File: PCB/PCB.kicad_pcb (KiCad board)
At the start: 2 copper layers, 110 x 80 mm, 109 parts, among them J2 Conn, J3 Screw_Terminal_01x02, J4 Screw_Terminal_01x02, J5 Screw_Terminal_01x02, J6 Screw_Terminal_01x02, Q1 Q_NPN_BCE, Q10 Q_NPN, Q11 Q_PNP_BCE, Q12 Q_NPN, Q13 Q_PNP, Q14 Q_PNP_BCE, Q15 Q_PNP_BCE, Q16 Q-NPN, Q17 Q-NPN, Q18 Q-NPN, Q19 Q-PNP, Q2 Q_PNP_BCE, Q20 Q-NPN, Q21 Q-PNP, Q22 Q-NPN, Q23 Q-PNP, Q24 Q-PNP, Q25 Q-NPN, Q26 Q-NPN, Q27 Q-PNP, Q28 Q-NPN, Q29 Q_PNP, Q3 Q_NPN_BCE, Q4 Q_PNP_BCE, Q5 Q_NPN_BCE, Q6 Q_PNP_BCE, Q7 Q_PNP_BCE, Q8 Q_NPN_BCE, Q9 Q_NPN_BCE

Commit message: update
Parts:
- moved Q2 2.00 mm to (186.0, 93.5), turned to 90 degrees
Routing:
- net Net-(C10-Pad1): track 16.8 -> 24.7 mm
- net Net-(C3-Pad1): track 33.5 -> 31.1 mm
- net Net-(Q2-Pad3): track 3.41 -> 5.24 mm
- net Net-(Q2-Pad1): track 19.2 -> 18.2 mm
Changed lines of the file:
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@@
     (thickness 1.6)
     (drawings 6)
-    (tracks 624)
+    (tracks 630)
     (zones 0)
     (modules 109)
@@
   )
   (setup
-    (last_trace_width 0.8)
+    (last_trace_width 0.4)
     (user_trace_width 0.4)
     (user_trace_width 0.8)
@@
   )
   (module Package_TO_SOT_SMD:SOT-23_Handsoldering (layer F.Cu)
-    (at 186 91.5)
+    (at 186 93.5 90)
     (descr "SOT-23, Handsoldering")
     (tags SOT-23)
     (attr smd)
-    (fp_text reference Q2 (at 0 -2.5) (layer F.SilkS)
+    (fp_text reference Q2 (at 0 -2.5 90) (layer F.SilkS)
       (effects (font (size 1 1) (thickness 0.15)))
     )
-    (fp_text value Q_PNP_BCE (at 0 2.5) (layer F.Fab)
+    (fp_text value Q_PNP_BCE (at 0 2.5 90) (layer F.Fab)
       (effects (font (size 1 1) (thickness 0.15)))
     )
@@
     (fp_line (start 0.76 -1.58) (end 0.76 -0.65) (layer F.SilkS) (width 0.12))
     (fp_line (start 0.76 1.58) (end 0.76 0.65) (layer F.SilkS) (width 0.12))
-    (fp_text user %R (at 0 0 90) (layer F.Fab)
+    (fp_text user %R (at 0 0) (layer F.Fab)
       (effects (font (size 0.5 0.5) (thickness 0.075)))
     )
-    (pad 3 smd rect (at 1.5 0) (size 1.9 0.8) (layers F.Cu F.Paste F.Mask)
+    (pad 3 smd rect (at 1.5 0 90) (size 1.9 0.8) (layers F.Cu F.Paste F.Mask)
       (net 34 "Net-(Q2-Pad3)"))
-    (pad 2 smd rect (at -1.5 0.95) (size 1.9 0.8) (layers F.Cu F.Paste F.Mask)
+    (pad 2 smd rect (at -1.5 0.95 90) (size 1.9 0.8) (layers F.Cu F.Paste F.Mask)
       (net 6 "Net-(C3-Pad1)"))
-    (pad 1 smd rect (at -1.5 -0.95) (size 1.9 0.8) (layers F.Cu F.Paste F.Mask)
+    (pad 1 smd rect (at -1.5 -0.95 90) (size 1.9 0.8) (layers F.Cu F.Paste F.Mask)
       (net 35 "Net-(Q2-Pad1)"))
     (model ${KISYS3DMOD}/Package_TO_SOT_SMD.3dshapes/SOT-23.wrl
@@
   (segment (start 188.8513 97.6013) (end 190.8987 97.6013) (width 0.4) (layer F.Cu) (net 6))
   (segment (start 197.5287 97.6013) (end 190.8987 97.6013) (width 0.8) (layer F.Cu) (net 6))
-  (segment (start 190.8987 97.6013) (end 186.8999 97.6013) (width 0.8) (layer F.Cu) (net 6))
   (segment (start 188.4513 97.6013) (end 188.8513 97.6013) (width 0.8) (layer F.Cu) (net 6))
-  (segment (start 184.5 93.65) (end 188.4513 97.6013) (width 0.8) (layer F.Cu) (net 6))
-  (segment (start 184.5 92.45) (end 184.5 93.65) (width 0.8) (layer F.Cu) (net 6))
+  (segment (start 189.6013 96.4513) (end 189.6013 97.6013) (width 0.8) (layer F.Cu) (net 6))
+  (segment (start 188.15 95) (end 189.6013 96.4513) (width 0.8) (layer F.Cu) (net 6))
+  (segment (start 186.95 95) (end 188.15 95) (width 0.8) (layer F.Cu) (net 6))
+  (segment (start 190.8987 97.6013) (end 189.6013 97.6013) (width 0.8) (layer F.Cu) (net 6))
+  (segment (start 189.6013 97.6013) (end 186.8999 97.6013) (width 0.8) (layer F.Cu) (net 6))
   (segment (start 203.384828 91.991772) (end 204.0082 91.3684) (width 0.8) (layer F.Cu) (net 7))
   (segment (start 203.377428 91.999172) (end 203.384828 91.991772) (width 0.4) (layer F.Cu) (net 7))
@@
   (segment (start 178.4341 104.923) (end 178.405 104.9521) (width 0.4) (layer F.Cu) (net 17))
   (segment (start 178.4341 101.1421) (end 178.4341 104.923) (width 0.8) (layer F.Cu) (net 17))
-  (segment (start 180.5513 99.0249) (end 178.4341 101.1421) (width 0.8) (layer F.Cu) (net 17))
-  (segment (start 180.5513 92.3881) (end 180.5513 99.0249) (width 0.8) (layer F.Cu) (net 17))
   (segment (start 178.4073 101.1153) (end 178.4341 101.1421) (width 0.8) (layer F.Cu) (net 17))
   (segment (start 175.0878 101.1153) (end 178.4073 101.1153) (width 0.8) (layer F.Cu) (net 17))
+  (segment (start 181.5 97.5) (end 178.5 100.5) (width 0.4) (layer F.Cu) (net 17))
+  (segment (start 181.813199 93.649999) (end 185.770001 93.649999) (width 0.4) (layer F.Cu) (net 17))
+  (segment (start 180.5513 92.3881) (end 181.813199 93.649999) (width 0.4) (layer F.Cu) (net 17))
+  (segment (start 185.770001 93.649999) (end 185.850001 93.729999) (width 0.4) (layer F.Cu) (net 17))
+  (segment (start 185.850001 93.729999) (end 185.850001 96.270001) (width 0.4) (layer F.Cu) (net 17))
+  (segment (start 185.850001 96.270001) (end 184.620002 97.5) (width 0.4) (layer F.Cu) (net 17))
+  (segment (start 184.620002 97.5) (end 181.5 97.5) (width 0.4) (layer F.Cu) (net 17))
   (segment (start 257.6872 61.3783) (end 260.5717 61.3783) (width 3) (layer F.Cu) (net 18))
   (segment (start 265.2 56.75) (end 274.7 56.75) (width 3) (layer F.Cu) (net 18))
@@
   (segment (start 184.7423 108.4954) (end 184.7423 104.4441) (width 0.8) (layer F.Cu) (net 33))
   (segment (start 190.7903 91.5) (end 190.8764 91.4139) (width 0.8) (layer F.Cu) (net 34))
-  (segment (start 187.5 91.5) (end 190.7903 91.5) (width 0.8) (layer F.Cu) (net 34))
+  (segment (start 190.2903 92) (end 190.8764 91.4139) (width 0.8) (layer F.Cu) (net 34))
+  (segment (start 186 92) (end 190.2903 92) (width 0.8) (layer F.Cu) (net 34))
   (segment (start 173.1878 95.7675) (end 173.198 95.7573) (width 0.4) (layer F.Cu) (net 35))
   (segment (start 173.1878 101.1153) (end 173.1878 95.7675) (width 0.8) (layer F.Cu) (net 35))
@@
   (segment (start 173.198 95.7573) (end 175.098 95.7573) (width 0.8) (layer F.Cu) (net 35))
   (segment (start 175.098 95.2073) (end 175.098 95.7573) (width 0.4) (layer F.Cu) (net 35))
-  (segment (start 178.89221 91.41309) (end 175.098 95.2073) (width 0.4) (layer F.Cu) (net 35))
-  (segment (start 181.170566 91.41309) (end 178.89221 91.41309) (width 0.4) (layer F.Cu) (net 35))
-  (segment (start 182.033656 90.55) (end 181.170566 91.41309) (width 0.4) (layer F.Cu) (net 35))
-  (segment (start 184.5 90.55) (end 182.033656 90.55) (width 0.4) (layer F.Cu) (net 35))
+  (segment (start 184.2927 95.7573) (end 185.05 95) (width 0.8) (layer F.Cu) (net 35))
+  (segment (start 175.098 95.7573) (end 184.2927 95.7573) (width 0.8) (layer F.Cu) (net 35))
   (segment (start 174.9378 110.3586) (end 174.9669 110.3877) (width 0.4) (layer F.Cu) (net 36))
   (segment (start 174.1378 110.3586) (end 174.9378 110.3586) (width 0.4) (layer F.Cu) (net 36))

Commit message: update pcb
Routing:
- net Net-(Q24-Pad3): track 49.8 -> 36.4 mm
- net Net-(Q19-Pad3): track 31.2 -> 20.7 mm
- net VCC: track 163.6 -> 169.1 mm
- net Net-(Q16-Pad1): track 23.3 -> 28.6 mm
- net Net-(C3-Pad1): track 31.1 -> 27.5 mm
- net GND: vias 1 -> 2

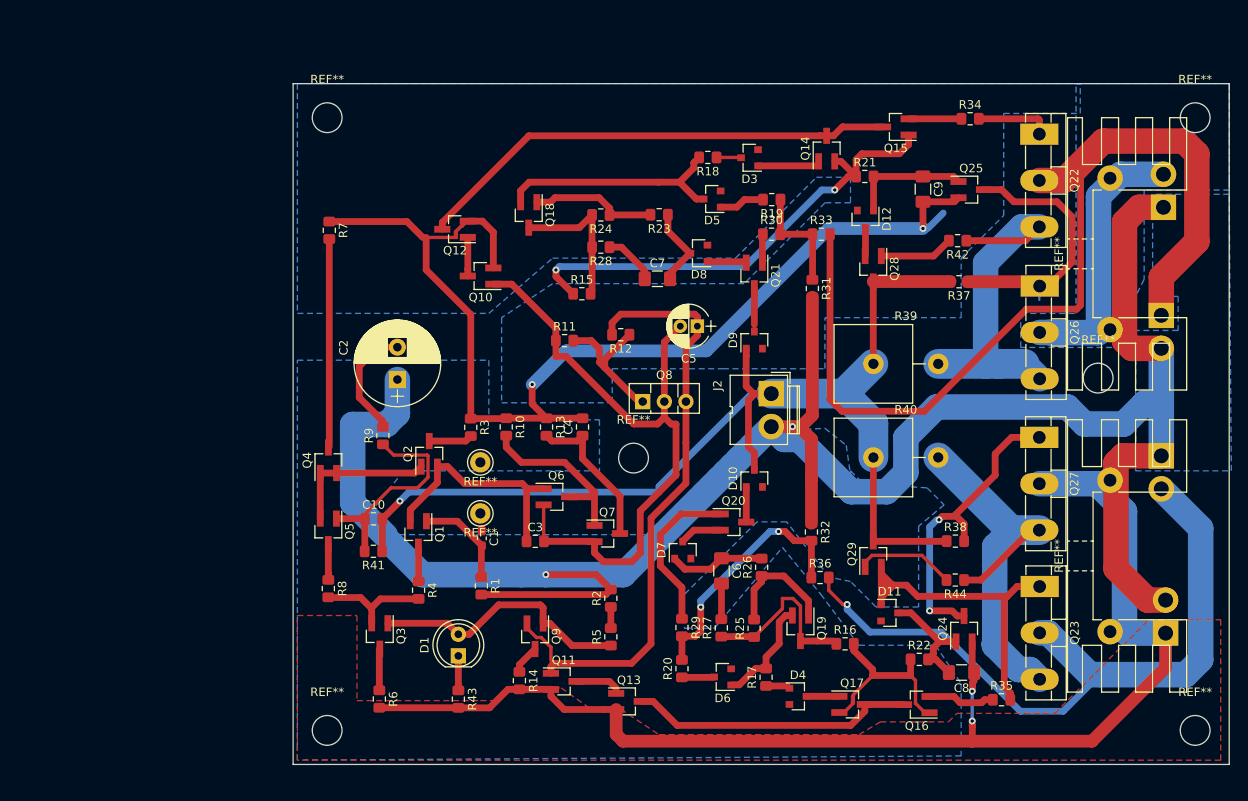
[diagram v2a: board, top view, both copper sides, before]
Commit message: Agregados los capacitores de alimentacion, pistas a las borneras sobre cara superior y a capacitores por cara inferior. Faltaría acomodar los FILL
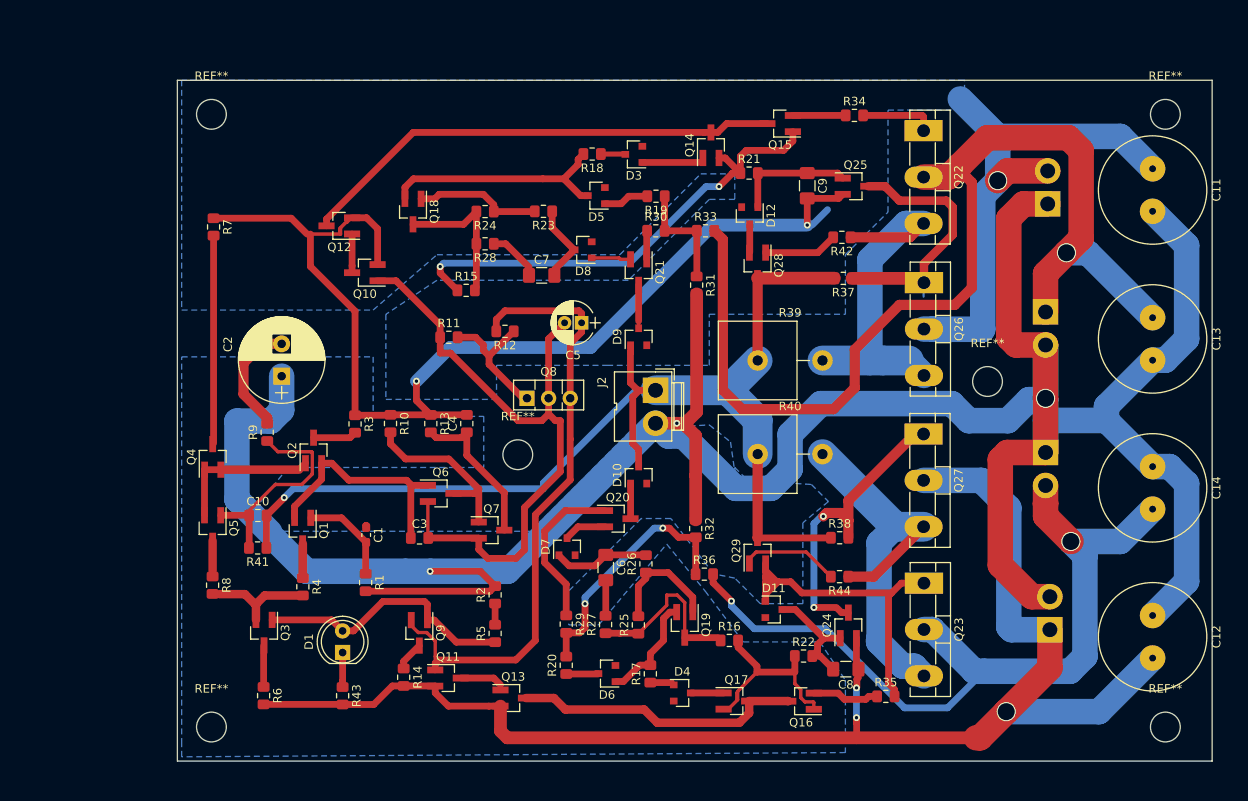
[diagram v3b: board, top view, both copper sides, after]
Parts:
- removed the REF** at (192.0, 94.5)
- removed the REF** at (192.0, 100.5)
- removed the REF** at (266.0, 105.5)
- removed the REF** at (266.0, 70.0)
- added C11: C, Capacitor_THT:C_Radial_D12.5mm_H20.0mm_P5.00mm, F.Cu at (271.0, 60.0)
- added C12: C, Capacitor_THT:C_Radial_D12.5mm_H20.0mm_P5.00mm, F.Cu at (271.0, 112.5)
- added C13: C, Capacitor_THT:C_Radial_D12.5mm_H20.0mm_P5.00mm, F.Cu at (271.0, 77.5)
- added C14: C, Capacitor_THT:C_Radial_D12.5mm_H20.0mm_P5.00mm, F.Cu at (271.0, 95.0)
- moved J4 13.6 mm to (258.9, 114.2)
- moved C1 13.6 mm to (178.6, 103.0)
- moved C10 13.6 mm to (165.9, 100.7)
- moved C3 13.6 mm to (184.9, 103.4)
- moved C5 13.6 mm to (203.9, 78.1)
- moved C7 13.6 mm to (199.2, 72.5)
- moved C8 13.6 mm to (235.0, 118.8)
- moved C9 13.6 mm to (230.4, 62.0)
- moved D10 13.6 mm to (210.6, 96.0)
- moved D12 13.6 mm to (223.7, 65.5)
- moved D3 13.6 mm to (210.0, 58.3)
- moved D4 13.6 mm to (215.7, 121.6)
- moved D5 13.6 mm to (205.6, 63.2)
- moved D6 13.6 mm to (206.9, 119.3)
- moved D7 13.6 mm to (202.2, 104.4)
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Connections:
- J5 pad 1: Net-(J5-Pad1) -> GND
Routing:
- net GND: track 275.0 -> 355.5 mm, vias 2 -> 3
- net VCC: track 169.1 -> 200.1 mm, vias 2 -> 3
- net VEE: track 147.9 -> 167.9 mm, vias 2 -> 3
- net +15V: track 112.7 -> 129.1 mm, vias 0 -> 1
- net -15V: track 85.0 -> 95.9 mm, vias 1 -> 2
- net Net-(Q23-Pad3): track 50.5 -> 51.5 mm
- net Net-(Q8-Pad1): track 17.1 -> 16.2 mm
- net Net-(Q24-Pad3): track 36.4 -> 35.5 mm
- net Net-(Q16-Pad1): track 28.6 -> 29.4 mm
- removed copper zone on F.Cu, net VEE
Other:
- board size 110 x 80 mm -> 121.6 x 80 mm

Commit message: rellené capas de abajo
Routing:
- added copper zone on B.Cu, net +15V
- added copper zone on B.Cu, net -15V
- added copper zone on B.Cu, net VEE
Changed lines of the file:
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@@
-(kicad_pcb (version 20171130) (host pcbnew "(5.1.4)-1")
+(kicad_pcb (version 20171130) (host pcbnew "(5.1.2)-2")
   (general
     (thickness 1.6)
@@
   )
   (setup
-    (last_trace_width 0.8)
+    (last_trace_width 0.3)
     (user_trace_width 0.4)
     (user_trace_width 0.6)
@@
       )
     )
+  )
+  (zone (net 3) (net_name GND) (layer B.Cu) (hatch edge 0.508)
+    (connect_pads (clearance 0.508))
+    (min_thickness 0.254)
+    (fill yes (arc_segments 32) (thermal_gap 0.508) (thermal_bridge_width 0.508))
+    (polygon
+      (pts
+        (xy 254 64) (xy 255.5 62.5) (xy 276.5 62.5) (xy 276.5 115) (xy 267.5 115)
+        (xy 267.5 106.5) (xy 273.5 100.5) (xy 273.5 98) (xy 272.5 97) (xy 269.5 97)
+        (xy 266.5 94) (xy 255.5 94) (xy 255.5 79.5) (xy 269 79.5) (xy 270 80.5)
+        (xy 272 80.5) (xy 273.5 79) (xy 273.5 69.5) (xy 271 67) (xy 254 67)
+      )
+    )
+  )
+  (zone (net 58) (net_name -15V) (layer B.Cu) (hatch edge 0.508)
+    (connect_pads (clearance 0.508))
+    (min_thickness 0.254)
+    (fill yes (arc_segments 32) (thermal_gap 0.508) (thermal_bridge_width 0.508))
+    (polygon
+      (pts
+        (xy 248 91.5) (xy 254 91.5) (xy 254.5 91.5) (xy 254.5 95.5) (xy 267 95.5)
+        (xy 269.5 98) (xy 272.5 98) (xy 272.5 100.5) (xy 266.5 106.5) (xy 266.5 115.5)
+        (xy 266.5 117) (xy 262 121.5) (xy 250.5 121.5) (xy 247 125) (xy 237.5 125)
+        (xy 237.5 121) (xy 237.5 120.5) (xy 232 115) (xy 224 115) (xy 220 111)
+        (xy 221.5 109.5) (xy 225 113) (xy 232.5 113) (xy 232.5 102) (xy 234.5 100)
+        (xy 237 102.5) (xy 237 117) (xy 242 122) (xy 246.5 122) (xy 251 117.5)
+        (xy 261 117.5) (xy 262 116.5) (xy 262 106) (xy 259.5 103.5) (xy 256 103.5)
+        (xy 256 98) (xy 252 94) (xy 248 94)
+      )
+    )
+  )
+  (zone (net 3) (net_name GND) (layer B.Cu) (hatch edge 0.508)
+    (connect_pads (clearance 0.508))
+    (min_thickness 0.254)
+    (fill yes (arc_segments 32) (thermal_gap 0.508) (thermal_bridge_width 0.508))
+    (polygon
+      (pts
+        (xy 256.5 104.5) (xy 256.5 112) (xy 261 112) (xy 261 106.5) (xy 259 104.5)
+      )
+    )
+  )
+  (zone (net 14) (net_name VEE) (layer B.Cu) (hatch edge 0.508)
+    (connect_pads (clearance 0.508))
+    (min_thickness 0.254)
+    (fill yes (arc_segments 32) (thermal_gap 0.508) (thermal_bridge_width 0.508))
+    (polygon
+      (pts
+        (xy 253.5 122) (xy 251.5 122) (xy 248 125.5) (xy 235.5 125.5) (xy 235.5 128.5)
+        (xy 276.5 128.5) (xy 276.5 115.5) (xy 268.5 115.5) (xy 262 122) (xy 253 122)
+        (xy 255 124) (xy 255.5 124.5)
+      )
+    )
+  )
+  (zone (net 18) (net_name +15V) (layer B.Cu) (hatch edge 0.508)
+    (connect_pads (clearance 0.508))
+    (min_thickness 0.254)
+    (fill yes (arc_segments 32) (thermal_gap 0.508) (thermal_bridge_width 0.508))
+    (polygon
+      (pts
+        (xy 253.5 68) (xy 253.5 78.5) (xy 269 78.5) (xy 270.5 79.5) (xy 272 79.5)
+        (xy 273 78.5) (xy 273 70) (xy 270.5 68)
+      )
+    )
+  )
+  (zone (net 8) (net_name VCC) (layer B.Cu) (hatch edge 0.508)
+    (connect_pads (clearance 0.508))
+    (min_thickness 0.254)
+    (fill yes (arc_segments 32) (thermal_gap 0.508) (thermal_bridge_width 0.508))
+    (polygon
+      (pts
+        (xy 249 50.5) (xy 276.5 50.5) (xy 276.5 62) (xy 249 62)
+      )
+    )

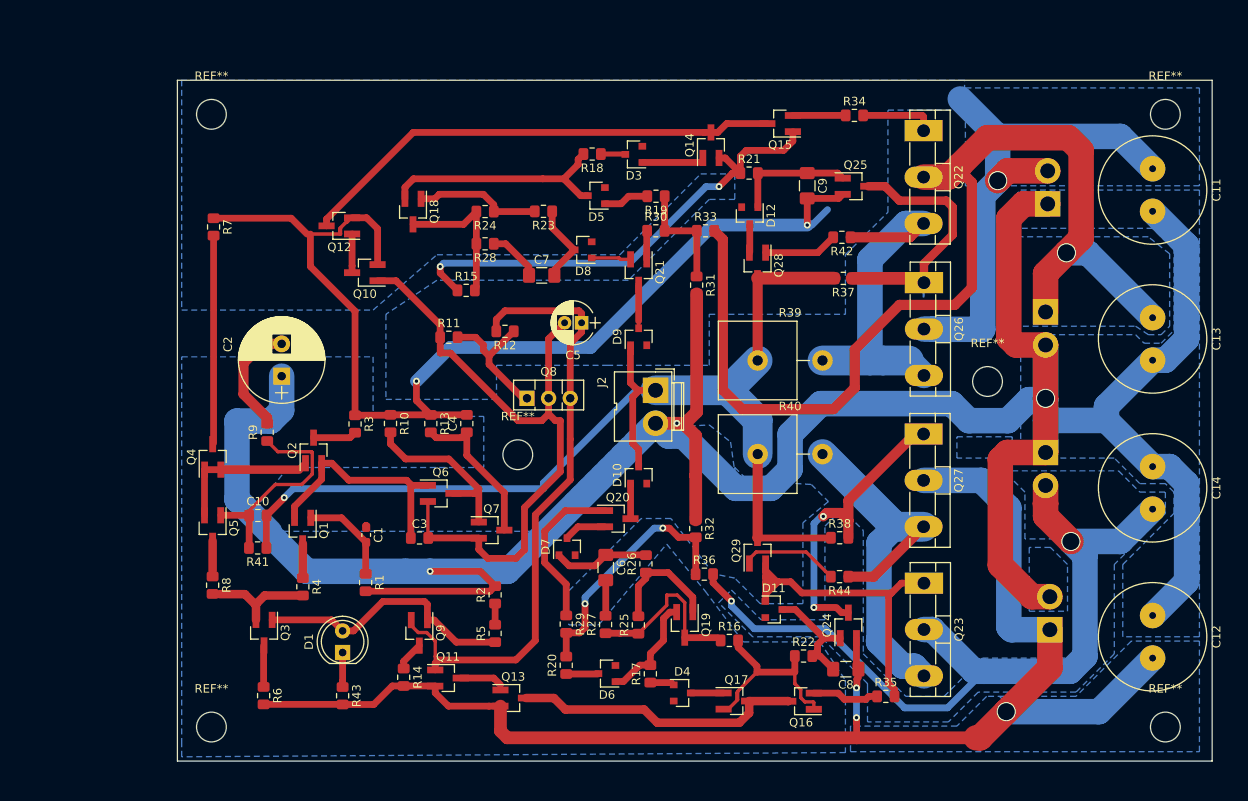
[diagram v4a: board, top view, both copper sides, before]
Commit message: Rellenos PROLIJOS, Jack 3.5mm
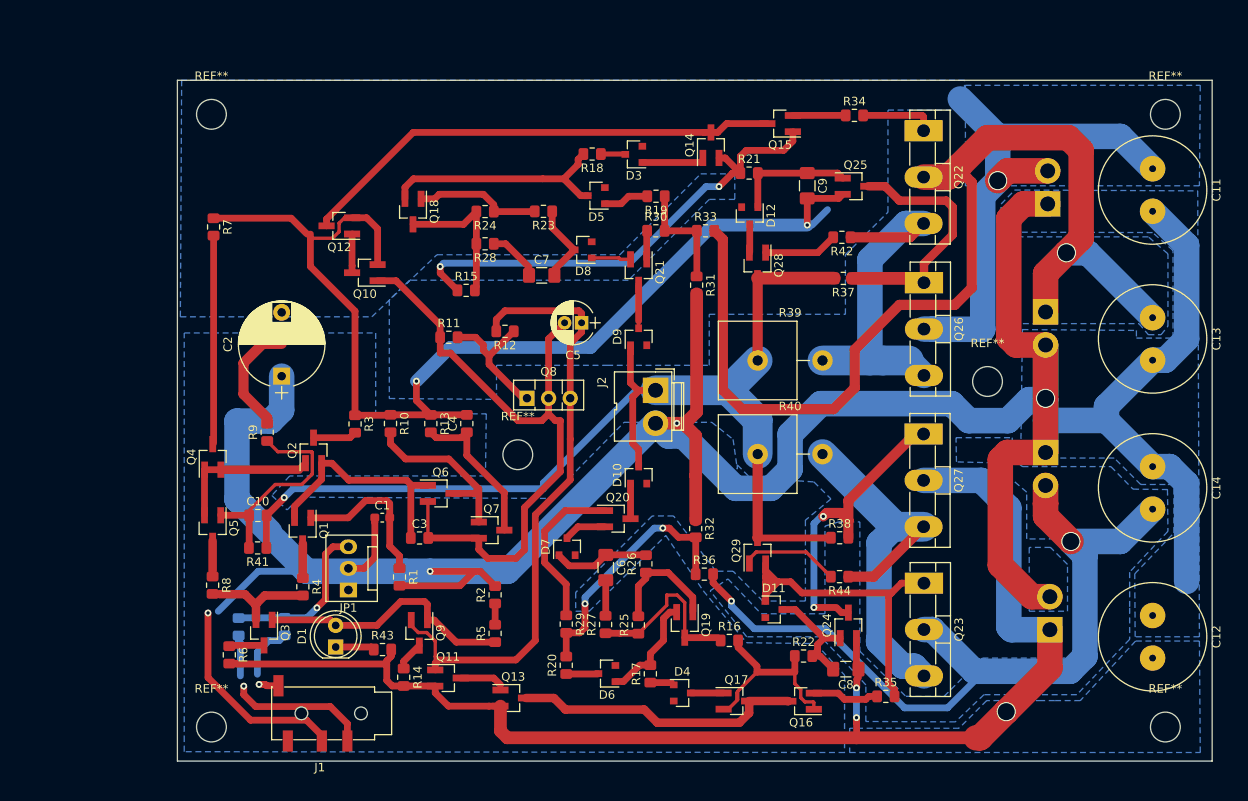
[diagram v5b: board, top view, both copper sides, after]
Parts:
- added J1: AudioJack3, Connector:PJ320D_3.5mm_Jack, F.Cu at (173.2, 124.0)
- added JP1: Jumper_3_Bridged12, Connector:Fan_Pin_Header_Straight_1x03, F.Cu at (176.5, 109.5)
- added R45: R, Resistor_SMD:R_0805_2012Metric_Pad1.15x1.40mm_HandSolder, B.Cu at (169.0, 113.8)
- added R46: R, Resistor_SMD:R_0805_2012Metric_Pad1.15x1.40mm_HandSolder, B.Cu at (163.6, 113.8)
- C2: footprint Capacitors_THT:CP_Radial_D10.0mm_P3.80mm -> Capacitors_THT:CP_Radial_D10.0mm_P7.50mm
- moved R43 7.17 mm to (180.5, 116.5), turned to 0 degrees
- moved R6 6.26 mm to (162.5, 117.1)
- moved R1 4.03 mm to (182.5, 108.0)
- moved C1 2.77 mm to (180.5, 101.0), turned to 0 degrees
- moved D1 1.04 mm to (175.0, 116.2)
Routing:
- net (no net): track 0.00 -> 43.4 mm, vias 0 -> 3
- net Net-(JP1-Pad3): track 0.00 -> 19.5 mm, vias 0 -> 1
- net VEE: track 167.9 -> 155.4 mm
- net Net-(C1-Pad1): track 0.51 -> 8.31 mm
- net Net-(C1-Pad2): track 11.4 -> 18.3 mm
- net Net-(J1-PadR): track 0.00 -> 6.62 mm
- net VCC: track 200.1 -> 195.2 mm
- net Net-(J1-PadS): track 0.00 -> 4.83 mm
- net Net-(Q25-Pad3): track 32.4 -> 30.9 mm
- net GND: track 355.5 -> 356.2 mm
- net Net-(Q3-Pad3): track 4.90 -> 4.19 mm
- net Net-(D1-Pad1): track 4.06 -> 4.60 mm
- net Net-(D1-Pad2): track 31.2 -> 30.7 mm

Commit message: update de lo charlado con edgar
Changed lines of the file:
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@@
   )
   (setup
-    (last_trace_width 0.8)
+    (last_trace_width 0.3)
     (user_trace_width 0.4)
     (user_trace_width 0.6)
@@
         (xy 223.7 96.3) (xy 231.2 96.8) (xy 233.2 98.8) (xy 230.2 101.3) (xy 230.2 110.8)
         (xy 225.2 110.8) (xy 221.69916 107.29624) (xy 219.7 107.3) (xy 214.7 100.8) (xy 212.19916 100.79624)
-        (xy 203.19916 109.79624) (xy 203.19916 111.99624) (xy 204.79874 111.99436) (xy 213.79916 103.09624) (xy 218.2 109.6)
-        (xy 223.3 115.7) (xy 231.4 115.8) (xy 234.8 119.5) (xy 234.8 128.6) (xy 157.2 128.5)
-        (xy 157.2 127.3)
+        (xy 203.19916 109.79624) (xy 203.19916 111.99624) (xy 203 112.5) (xy 203.5 113.5) (xy 203.5 115)
+        (xy 203 116.5) (xy 204 119.5) (xy 204 128.6) (xy 157.2 128.5) (xy 157.2 127.3)
       )
     )
@@
         (xy 268.3 115.3) (xy 262.1 121.8) (xy 251.1875 121.8) (xy 247.825 125) (xy 237.3 124.95)
         (xy 237.3 120.65) (xy 234.4 117.5) (xy 232 115) (xy 223.3 115) (xy 219 109.6)
-        (xy 221.1 108.2) (xy 225 112.3) (xy 232.5 112.3) (xy 232.5 102) (xy 234.1 101.5)
-        (xy 236.6 101.5) (xy 236.6 116.7) (xy 242 122) (xy 246.5 122) (xy 251 117.5)
+        (xy 221.1 108.2) (xy 225 112.3) (xy 232.5 112.3) (xy 233 112.5) (xy 233.75 112.5)
+        (xy 236.25 112.5) (xy 236.6 116.7) (xy 242 122) (xy 246.5 122) (xy 251 117.5)
         (xy 261 117.5) (xy 262 116.5) (xy 262 106) (xy 259.5 103.5) (xy 256.2 103.5)
         (xy 256.2 98) (xy 252.2 94.55) (xy 247.95 94.45)
